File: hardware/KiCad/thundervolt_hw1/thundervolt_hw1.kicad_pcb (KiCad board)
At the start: 4 copper layers, 46.9 x 54.8 mm, 59 parts, among them IC4 LP5907UVX-1.8_NOPB, U1 TPS628681ARQYR, U2 TPS628681ARQYR, U3 TPS628682ARQYR, U4 TPS63810YFFR, U5 ATTINY1616-MNR, U7 TMP1075NDRLR

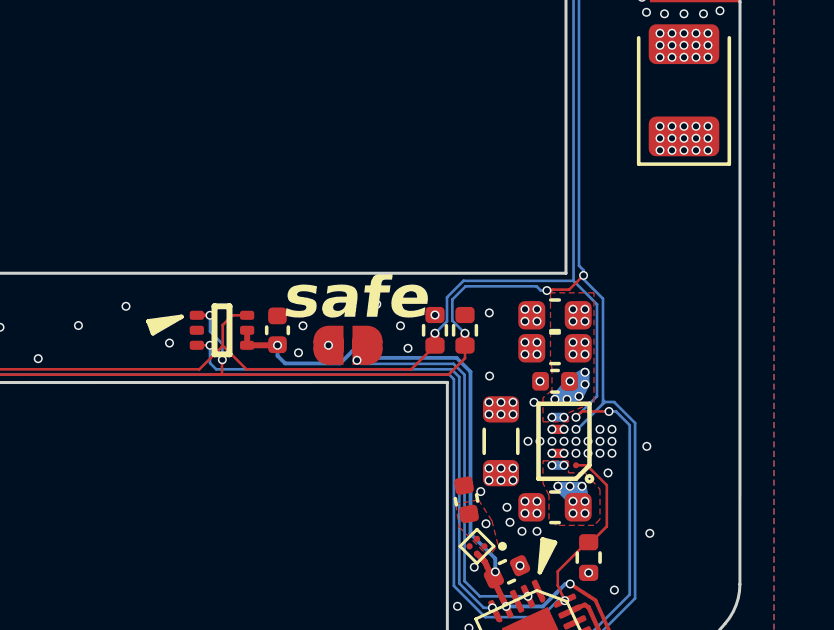
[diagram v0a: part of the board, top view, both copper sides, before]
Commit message: Remove HW2 gerbers and update HW1 gerbers
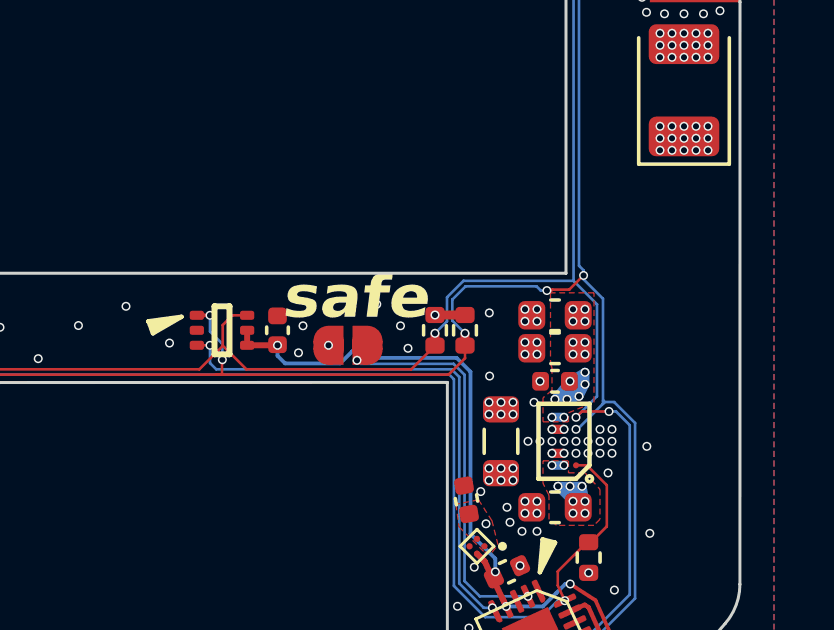
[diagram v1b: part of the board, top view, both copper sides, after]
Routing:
- net Net-(U4-LX2): track 21.4 -> 22.5 mm
- net Net-(U4-LX1): track 20.6 -> 21.7 mm
- net +1V8: track 69.3 -> 70.3 mm
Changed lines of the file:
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@@
 			(usegerberattributes yes)
 			(usegerberadvancedattributes yes)
-			(creategerberjobfile yes)
+			(creategerberjobfile no)
 			(dashed_line_dash_ratio 12.000000)
 			(dashed_line_gap_ratio 3.000000)
@@
 			(drillshape 0)
 			(scaleselection 1)
-			(outputdirectory "G:/thundervolt/KiCad/thundervolt/gerbers/")
+			(outputdirectory "../../gerbers/thundervolt_1/")
 		)
 	)
@@
 	)
 	(segment
+		(start 156.279802 103.476758)
+		(end 155.279802 103.476758)
+		(width 0.3)
+		(layer "F.Cu")
+		(net 3)
+	)
+	(segment
 		(start 126.404802 76.586758)
 		(end 126.404812 76.584898)
@@
 	)
 	(segment
+		(start 159.879802 109.686758)
+		(end 160.279802 109.686758)
+		(width 0.3)
+		(layer "In2.Cu")
+		(net 11)
+	)
+	(segment
 		(start 134.154163 110.888481)
 		(end 133.879802 111.786758)
@@
 	)
 	(segment
+		(start 157.479802 106.386758)
+		(end 157.079802 106.786758)
+		(width 0.3)
+		(layer "In2.Cu")
+		(net 13)
+	)
+	(segment
 		(start 157.079802 106.386758)
 		(end 157.079802 106.786758)
@@
 	)
 	(segment
+		(start 157.479802 106.786758)
+		(end 157.879802 106.386758)
+		(width 0.3)
+		(layer "In2.Cu")
+		(net 13)
+	)
+	(segment
 		(start 157.079802 106.786758)
 		(end 157.879802 106.786758)
@@
 	)
 	(segment
+		(start 157.879802 108.586758)
+		(end 157.479802 108.986758)
+		(width 0.3)
+		(layer "In2.Cu")
+		(net 14)
+	)
+	(segment
 		(start 157.079802 108.986758)
 		(end 157.079802 108.586758)
 		(width 0.3)
+		(layer "In2.Cu")
+		(net 14)
+	)
+	(segment
+		(start 157.479802 108.986758)
+		(end 157.079802 108.586758)
+		(width 0.3)
